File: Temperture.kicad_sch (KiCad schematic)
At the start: 6 parts

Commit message: Первый вариант
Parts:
- removed C46, C47, C48: 0.1u, Capacitor_SMD:C_0603_1608Metric_Pad1.08x0.95mm_HandSolder, symbol Device:C_Small
- removed D2, D3, D4: STLM75DS2F, Package_SO:MSOP-8_3x3mm_P0.65mm, symbol Temperature_My:STLM75DS2F
- added TH1, TH2: Thermistor_NTC, symbol Device:Thermistor_NTC
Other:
- note removed: "Адрес: 1001001"
- note removed: "Адрес: 1001010"
- note removed: "Адрес: 1001011"
- note removed: "Температура фазы А"
- note removed: "Температура фазы В"
- note removed: "Температура фазы С"

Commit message: Сохранил схему
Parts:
- removed TH1: Thermistor_NTC, symbol Device:Thermistor_NTC
- TH2: footprint (none) -> Resistor_SMD:R_0603_1608Metric_Pad0.98x0.95mm_HandSolder
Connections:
- net NTC+: now reaches TH2.1
- net NTC-: now reaches TH2.2
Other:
- moved on the sheet: TH2
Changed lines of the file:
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@@
-(kicad_sch (version 20230121) (generator eeschema)
-  (paper "A4")
-  (title_block
-    (company "Московский Политех")
-    (comment 1 "МПСТ.76721.758764.01.М Э3")
-  )
-  (symbol (lib_id "Device:Thermistor_NTC") (at 145.415 87.63 0) (unit 1)
-    (in_bom yes) (on_board yes) (dnp no) (fields_autoplaced)
-    (property "Reference" "TH1" (at 148.59 87.3124 0)
-      (effects (font (size 1.27 1.27)) (justify left))
-    )
-    (property "Value" "Thermistor_NTC" (at 148.59 89.8524 0)
-      (effects (font (size 1.27 1.27)) (justify left))
-    )
-    (property "Footprint" "" (at 145.415 86.36 0)
-      (effects (font (size 1.27 1.27)) hide)
-    )
-    (property "Datasheet" "~" (at 145.415 86.36 0)
-      (effects (font (size 1.27 1.27)) hide)
-    )
-    (pin "1")
-    (pin "2")
-    (instances
-      (project "Силовая плата"
-        (path "/96c6fc92-8ec6-44f7-b0dc-9ad8f1acea09/005a885b-ef5f-4b8c-934f-72ceac7d73e5"
-          (reference "TH1") (unit 1)
-        )
-      )
-    )
-  )
-  (symbol (lib_id "Device:Thermistor_NTC") (at 145.415 76.2 0) (unit 1)
-    (in_bom yes) (on_board yes) (dnp no) (fields_autoplaced)
-    (property "Reference" "TH2" (at 148.59 75.8824 0)
-      (effects (font (size 1.27 1.27)) (justify left))
-    )
-    (property "Value" "Thermistor_NTC" (at 148.59 78.4224 0)
-      (effects (font (size 1.27 1.27)) (justify left))
-    )
-    (property "Footprint" "" (at 145.415 74.93 0)
-      (effects (font (size 1.27 1.27)) hide)
-    )
-    (property "Datasheet" "~" (at 145.415 74.93 0)
-      (effects (font (size 1.27 1.27)) hide)
-    )
-    (pin "1")
-    (pin "2")
-    (instances
-      (project "Силовая плата"
-        (path "/96c6fc92-8ec6-44f7-b0dc-9ad8f1acea09/005a885b-ef5f-4b8c-934f-72ceac7d73e5"
-          (reference "TH2") (unit 1)
-        )
-      )
-    )
-  )
+(kicad_sch
+	(version 20231120)
+	(generator "eeschema")
+	(generator_version "8.0")
+	(paper "A4")
+	(title_block
+		(company "Московский Политех")
+		(comment 1 "МПСТ.76721.758764.01.М Э3")
+	)
+	(wire
+		(pts
+			(xy 144.78 80.01) (xy 144.78 81.28)
+		)
+		(stroke
+			(width 0)
+			(type default)
+		)
+	)
+	(wire
+		(pts
+			(xy 144.78 71.12) (xy 147.32 71.12)
+		)
+		(stroke
+			(width 0)
+			(type default)
+		)
+	)
+	(wire
+		(pts
+			(xy 144.78 71.12) (xy 144.78 72.39)
+		)
+		(stroke
+			(width 0)
+			(type default)
+		)
+	)
+	(wire
+		(pts
+			(xy 144.78 81.28) (xy 147.32 81.28)
+		)
+		(stroke
+			(width 0)
+			(type default)
+		)
+	)
+	(global_label "NTC-"
+		(shape input)
+		(at 147.32 81.28 0)
+		(fields_autoplaced yes)
+		(effects
+			(font
+				(size 1.27 1.27)
+			)
+			(justify left)
+		)
+		(property "Intersheetrefs" "${INTERSHEET_REFS}"
+			(at 153.8968 81.28 0)
+			(effects
+				(font
+					(size 1.27 1.27)
+				)
+				(justify left)
+				(hide yes)
+			)
+		)
+	)
+	(global_label "NTC+"
+		(shape input)
+		(at 147.32 71.12 0)
+		(fields_autoplaced yes)
+		(effects
+			(font
+				(size 1.27 1.27)
+			)
+			(justify left)
+		)
+		(property "Intersheetrefs" "${INTERSHEET_REFS}"
+			(at 153.8968 71.12 0)
+			(effects
+				(font
+					(size 1.27 1.27)
+				)
+				(justify left)
+				(hide yes)
+			)
+		)
+	)
+	(symbol
+		(lib_id "Device:Thermistor_NTC")
+		(at 144.78 76.2 0)
+		(unit 1)
+		(exclude_from_sim no)
+		(in_bom yes)
+		(on_board yes)
+		(dnp no)
+		(fields_autoplaced yes)
+		(property "Reference" "TH2"
+			(at 147.955 75.8824 0)
+			(effects
+				(font
+					(size 1.27 1.27)
+				)
+				(justify left)
+			)
+		)
+		(property "Value" "Thermistor_NTC"
+			(at 147.955 78.4224 0)
+			(effects
+				(font
+					(size 1.27 1.27)
+				)
+				(justify left)
+				(hide yes)
+			)
+		)
+		(property "Footprint" "Resistor_SMD:R_0603_1608Metric_Pad0.98x0.95mm_HandSolder"
+			(at 144.78 74.93 0)
+			(effects
+				(font
+					(size 1.27 1.27)
+				)
+				(hide yes)
+			)
+		)
+		(property "Datasheet" "~"
+			(at 144.78 74.93 0)
+			(effects
+				(font
+					(size 1.27 1.27)
+				)
+				(hide yes)
+			)
+		)
+		(property "Description" ""
+			(at 144.78 76.2 0)
+			(effects
+				(font
+					(size 1.27 1.27)
+				)
+				(hide yes)
+			)
+		)
+		(pin "1"
+		)
+		(pin "2"
+		)
+		(instances
+			(project "Силовая плата"
+				(path "/96c6fc92-8ec6-44f7-b0dc-9ad8f1acea09/005a885b-ef5f-4b8c-934f-72ceac7d73e5"
+					(reference "TH2")
+					(unit 1)
+				)
+			)
+		)
+	)
 )

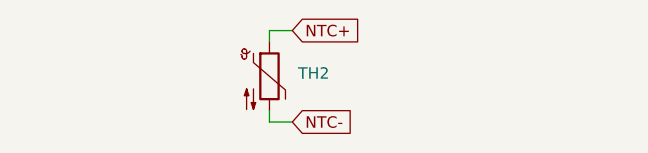
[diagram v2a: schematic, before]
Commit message: Заменил разъёмы 2.54 на 1.27мм
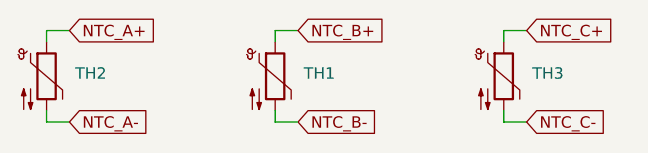
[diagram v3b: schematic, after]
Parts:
- added TH1, TH3: Thermistor_NTC, Resistor_SMD:R_0603_1608Metric_Pad0.98x0.95mm_HandSolder, symbol Device:Thermistor_NTC
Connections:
- net NTC+ renamed NTC_A+
- net NTC- renamed NTC_A-
- new net NTC_B+: TH1.1
- new net NTC_B-: TH1.2
- new net NTC_C+: TH3.1
- new net NTC_C-: TH3.2
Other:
- moved on the sheet: TH2

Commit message: Изменения: добавил папку с отчетностью
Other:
- note added: "Датчики температуры"
- moved on the sheet: TH1, TH2, TH3
